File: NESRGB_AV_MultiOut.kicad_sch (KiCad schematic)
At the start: 23 parts, among them X1 AFC07-S18ECA-00, Y0 SMD2

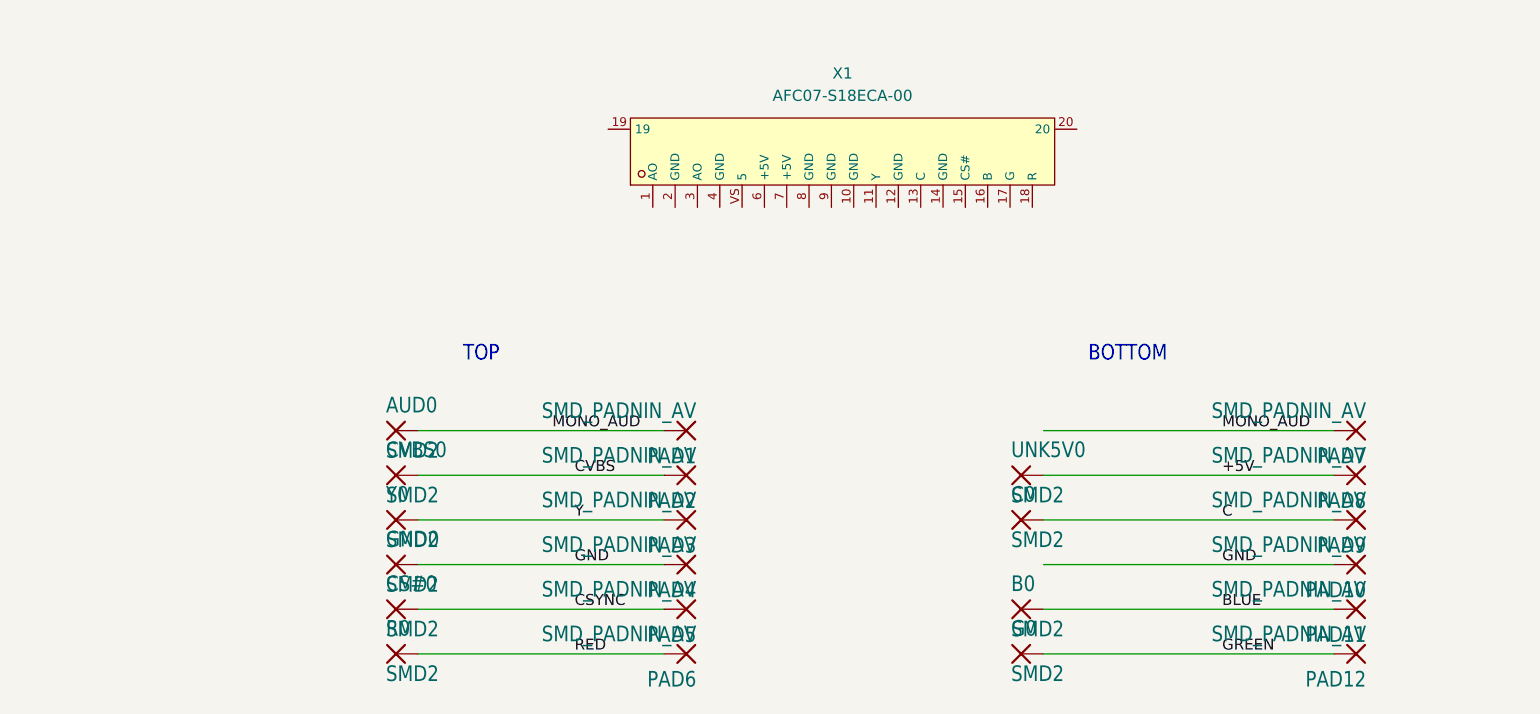
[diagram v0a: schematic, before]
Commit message: Create scripts for github ci and for creating fabrication outputs.
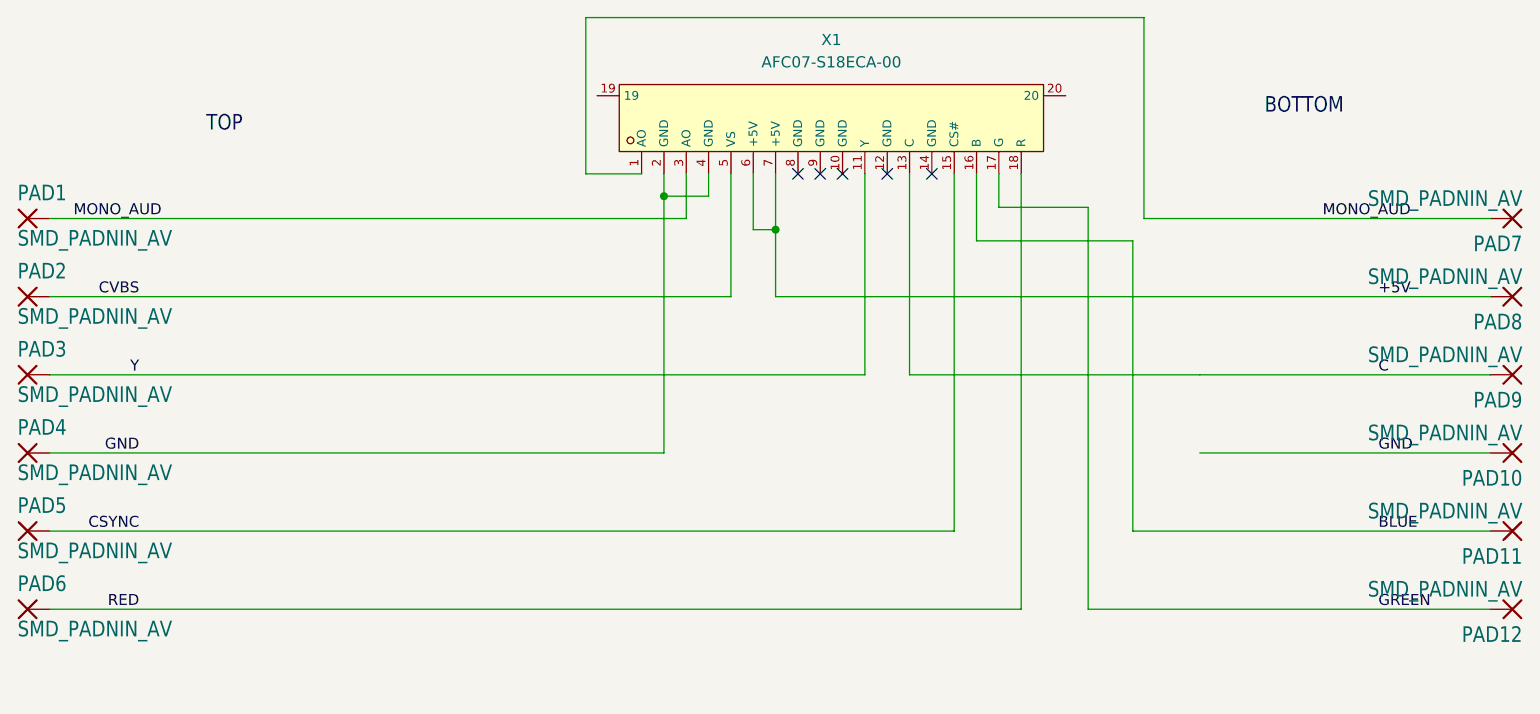
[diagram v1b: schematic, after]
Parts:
- removed AUD0, B0, C0, CS#0, CVBS0, G0, GND0, R0, UNK5V0, Y0: SMD2, NESRGB_AV_MultiOut:SMD1,27-2,54, symbol NESRGB_AV_MultiOut-eagle-import:SMD2
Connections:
- net +5V: now also X1.6 (+5V), X1.7 (+5V)
- net BLUE: now also X1.16 (B)
- net C: now also X1.13 (C)
- net CSYNC: now also X1.15 (CS#)
- net CVBS: now also X1.5 (VS)
- net GND: now also X1.2 (GND), X1.4 (GND)
- net GREEN: now also X1.17 (G)
- net MONO_AUD: now also X1.1 (AO), X1.3 (AO)
- net RED: now also X1.18 (R)
- net Y: now also X1.11 (Y)
- no-connect marks 0 -> 5
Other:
- moved on the sheet: PAD1, PAD10, PAD11, PAD12, PAD2, PAD3, PAD4, PAD5, PAD6, PAD7, PAD8, PAD9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

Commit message: Added checks for erc/drc in github ci. Added badges to README. Cleaned up all erc/drc, all clean.
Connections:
- net GND: now also X1.10 (GND), X1.12 (GND), X1.14 (GND), X1.8 (GND), X1.9 (GND)
- no-connect marks 5 -> 2
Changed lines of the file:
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@@
+	)
+	(junction
+		(at 147.32 71.12)
+		(diameter 0)
+		(color 0 0 0 0)
 	)
 	(junction
@@
 		(color 0 0 0 0)
 	)
+	(junction
+		(at 139.7 64.77)
+		(diameter 0)
+		(color 0 0 0 0)
+	)
 	(no_connect
-		(at 152.4 64.77)
+		(at 114.3 55.88)
 	)
 	(no_connect
-		(at 139.7 64.77)
-	)
-	(no_connect
-		(at 137.16 64.77)
-	)
-	(no_connect
-		(at 147.32 64.77)
-	)
-	(no_connect
-		(at 142.24 64.77)
+		(at 167.64 55.88)
 	)
 	(wire
@@
 	(wire
 		(pts
+			(xy 147.32 96.52) (xy 147.32 71.12)
+		)
+		(stroke
+			(width 0.1524)
+			(type solid)
+		)
+	)
+	(wire
+		(pts
 			(xy 170.18 68.58) (xy 160.02 68.58)
 		)
@@
 	(wire
 		(pts
+			(xy 139.7 71.12) (xy 147.32 71.12)
+		)
+		(stroke
+			(width 0)
+			(type default)
+		)
+	)
+	(wire
+		(pts
 			(xy 52.07 114.3) (xy 162.56 114.3)
 		)
@@
 	(wire
 		(pts
+			(xy 147.32 71.12) (xy 147.32 64.77)
+		)
+		(stroke
+			(width 0.1524)
+			(type solid)
+		)
+	)
+	(wire
+		(pts
 			(xy 160.02 68.58) (xy 160.02 64.77)
 		)
@@
 	(wire
 		(pts
+			(xy 152.4 71.12) (xy 147.32 71.12)
+		)
+		(stroke
+			(width 0)
+			(type default)
+		)
+	)
+	(wire
+		(pts
 			(xy 170.18 114.3) (xy 170.18 68.58)
 		)
@@
 	(wire
 		(pts
+			(xy 139.7 64.77) (xy 139.7 71.12)
+		)
+		(stroke
+			(width 0)
+			(type default)
+		)
+	)
+	(wire
+		(pts
 			(xy 154.94 105.41) (xy 154.94 64.77)
 		)
@@
 	(wire
 		(pts
+			(xy 147.32 96.52) (xy 215.9 96.52)
+		)
+		(stroke
+			(width 0.1524)
+			(type solid)
+		)
+	)
+	(wire
+		(pts
+			(xy 139.7 64.77) (xy 142.24 64.77)
+		)
+		(stroke
+			(width 0)
+			(type default)
+		)
+	)
+	(wire
+		(pts
 			(xy 52.07 69.85) (xy 124.46 69.85)
 		)
@@
 	(wire
 		(pts
+			(xy 137.16 64.77) (xy 139.7 64.77)
+		)
+		(stroke
+			(width 0)
+			(type default)
+		)
+	)
+	(wire
+		(pts
 			(xy 176.53 46.99) (xy 113.03 46.99)
 		)
@@
 	(wire
 		(pts
-			(xy 182.88 96.52) (xy 215.9 96.52)
-		)
-		(stroke
-			(width 0.1524)
-			(type solid)
-		)
-	)
+			(xy 152.4 64.77) (xy 152.4 71.12)
+		)
+		(stroke
+			(width 0)
+			(type default)
+		)
+	)
